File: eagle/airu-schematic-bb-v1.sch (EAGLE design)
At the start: 24 parts, among them Q2 MOSFET-NCHANNELAO3404A, U1 BMP180, U2 DHT22, U3 GPS, X2 53261-08

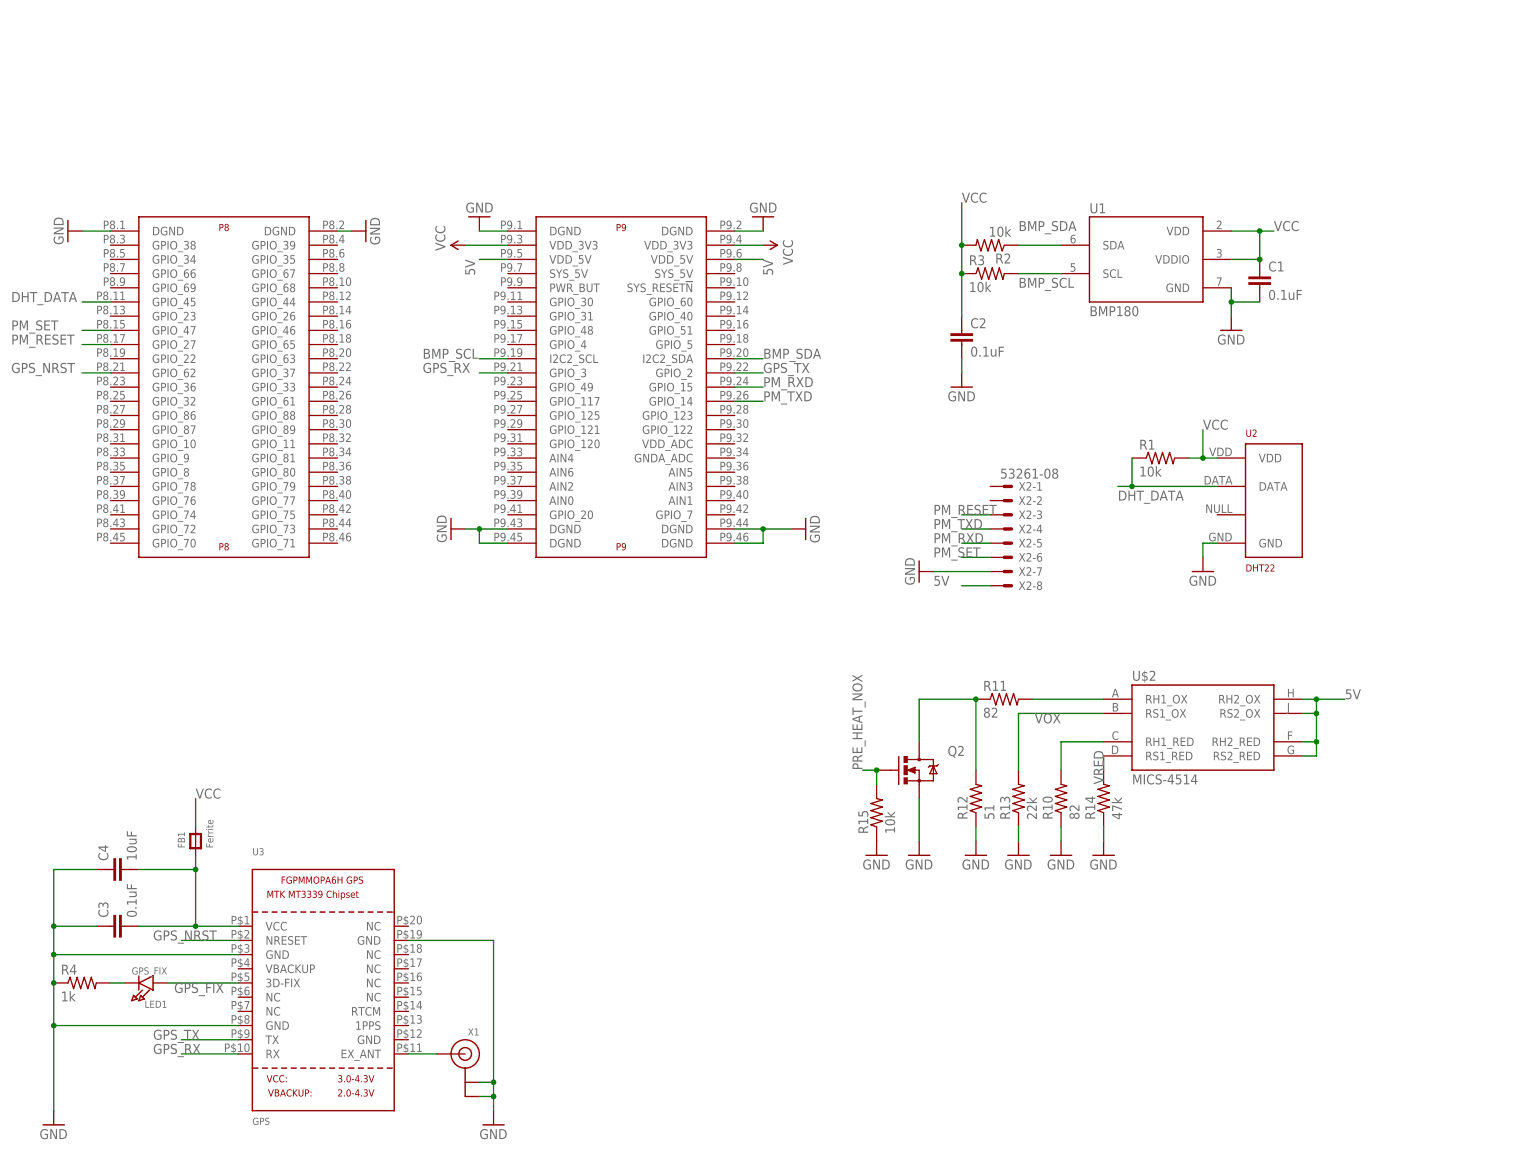
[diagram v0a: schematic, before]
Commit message: Finalized AirU schematic and board V1.0!
This commit includes the last changes for V1.0 of the AirU air quality board.
These changes include:

1. Bill of Materials
2. Final schematic
3. Final board layout
4. PDFs of the schematic and board layout.
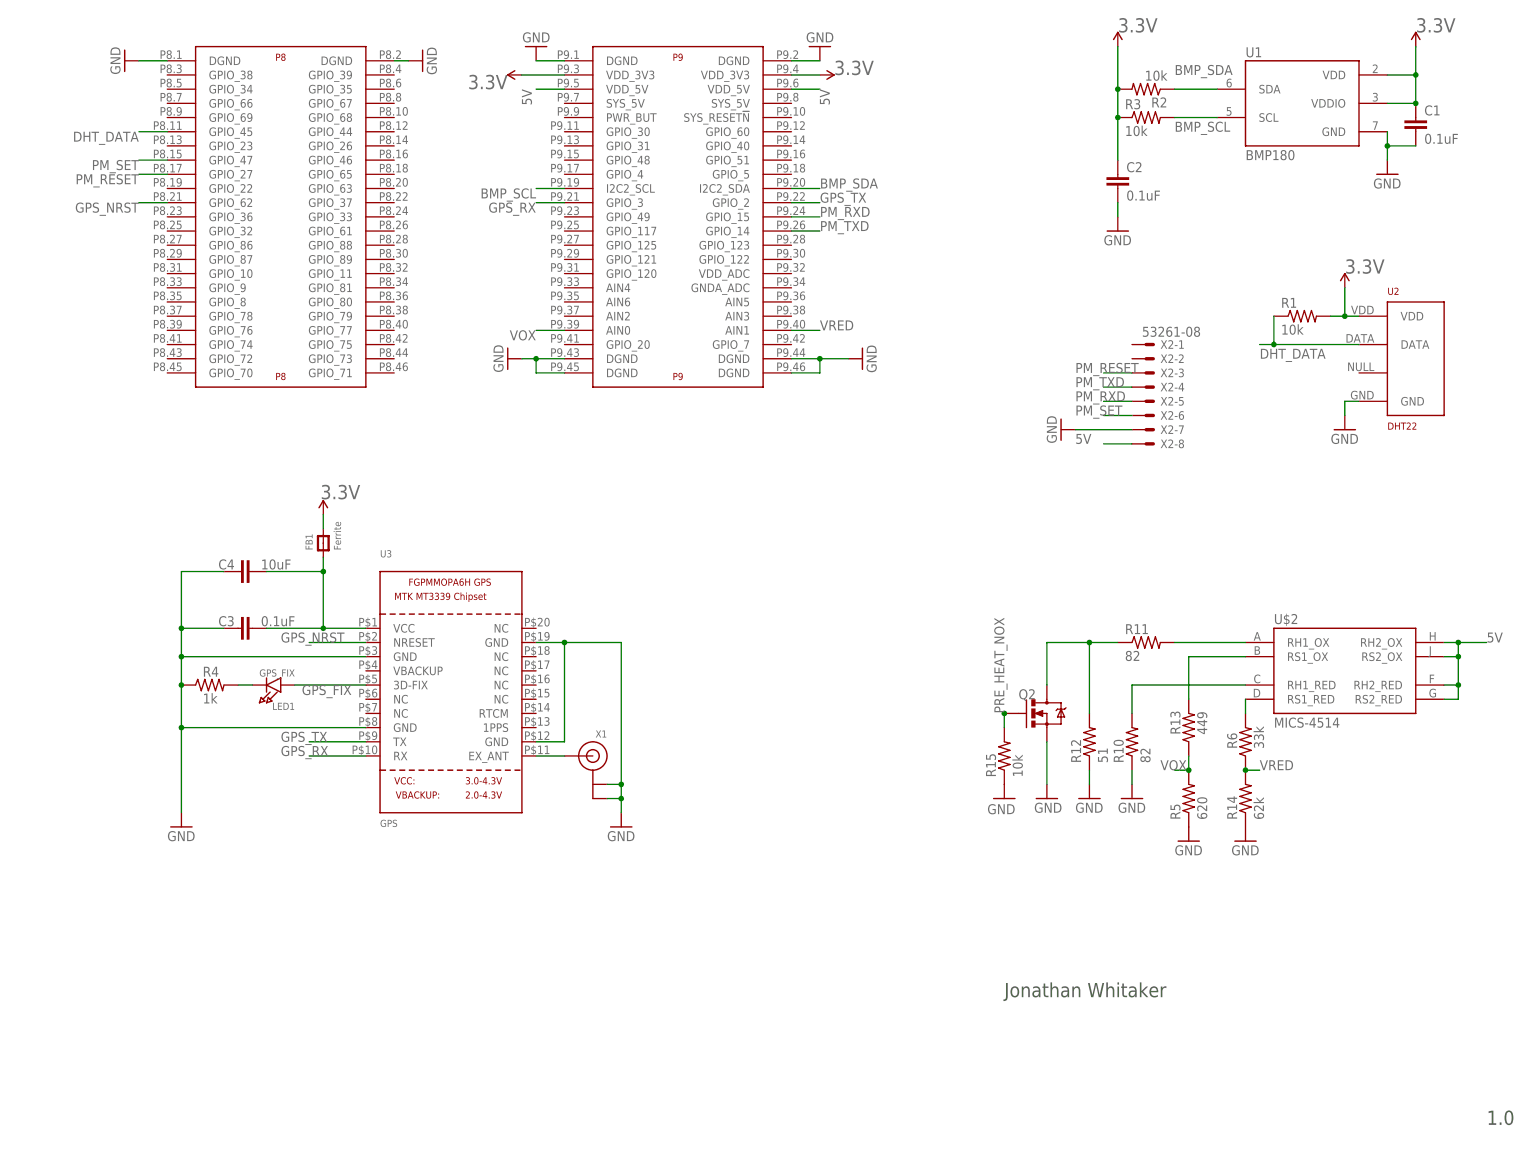
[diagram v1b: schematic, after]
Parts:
- added R5: 620, SparkFun-Passives:RESISTOR1206
- added R6: 33k, SparkFun-Passives:RESISTOR1206
- R13: value 22k -> 449
- R14: value 47k -> 62k
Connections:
- net VCC renamed 3.3V
- new net N$6: R13.2, U$2.RS1_OX
- new net N$8: R6.2, U$2.RS1_RED
- net GND: now also R5.1, U3.GND@3; no longer R13.1
- net VOX: now also R13.1, R5.2, U$1P9.AIN0; no longer R13.2, U$2.RS1_OX
- net VRED: now also R6.1, U$1P9.AIN1; no longer U$2.RS1_RED
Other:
- note added: "1.0"
- note added: "Jonathan Whitaker"
- moved on the sheet: C1, C2, C3, C4, FB1, LED1, Q2, R1, R10, R11, R12, R13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

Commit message: Made improvements to layout and added silkscreen components.
This commit includes improvments to the physical layout as well as
comments on the silkscreen layer.
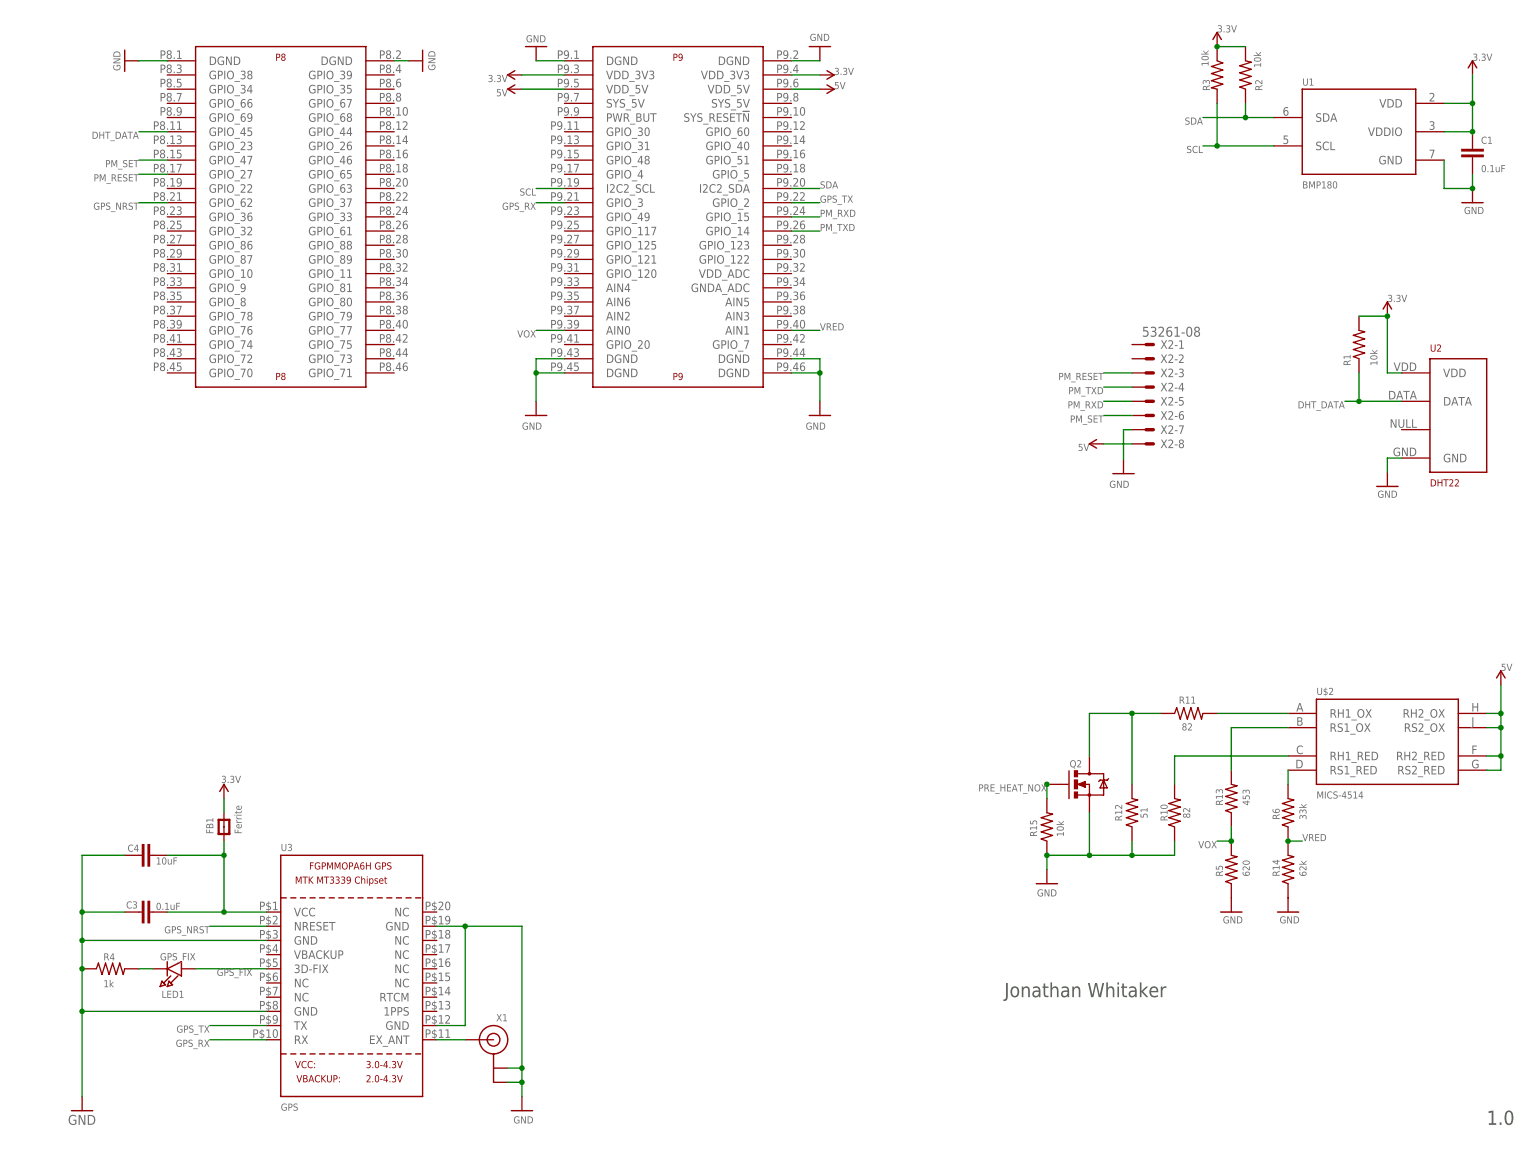
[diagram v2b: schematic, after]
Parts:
- removed C2: 0.1uF, SparkFun-Passives:CAP1206
- R13: value 449 -> 453
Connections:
- net BMP_SCL renamed SCL
- net BMP_SDA renamed SDA
- net 3.3V: no longer C2.1
- net GND: no longer C2.2
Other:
- note added: "CO/NO2 MODULE"
- note added: "GPS MODULE"
- note added: "PM1/2.5/10 MODULE"
- note added: "PRESSURE/TEMP/ALT MODULE"
- note added: "TEMP/HUMIDITY MODULE"
- moved on the sheet: C1, C3, C4, FB1, LED1, Q2, R1, R10, R11, R12, R13, R14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
